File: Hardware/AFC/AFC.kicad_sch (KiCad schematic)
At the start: 102 parts, among them J1 Barrel_Jack_Switch, J2 Conn_Coaxial, J3 Conn_Coaxial, J4 Conn_Coaxial, J5 Conn_Coaxial, J7 Conn_Coaxial, J8 Conn_Coaxial, U1 AD633JRZ, U10 MC79M12_TO252, U11 LF120_TO252, U12 AD8429, U2 AD633JRZ, U3 AD630ARZ, U4 AD8429, U5 AD8429, U6 LM358, U7 LM358, U8 LM358, U9 LMV358

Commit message: Updates to schematic
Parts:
- removed J5: Conn_Coaxial, symbol Connector:Conn_Coaxial
- added C41: 100nF, symbol Device:C_Small
- R34, R5, R6: value 10k -> 100k
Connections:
- net Conventional: now also C41.1; no longer R34.2, U12.4 (+)
- net at R31.1, RV1.2, U8.6 (-): no longer RV1.1
- new net: C41.2, R34.2, U12.4 (+)
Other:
- note added: "Low Pass Filter and Output"
- note added: "Op Amp Power Supplies"
- note added: "Power Input and Regulation"
- company: (none) -> openEPR
- title: (none) -> AFC
- moved on the sheet: C23, C24, J7, J8, R12, R13, R14, R15, R16, R17, R18, R19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

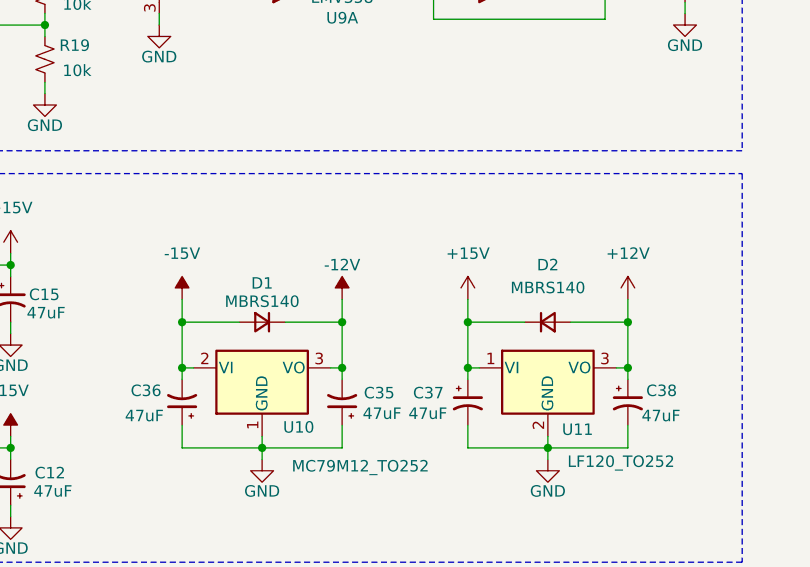
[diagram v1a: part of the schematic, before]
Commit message: Adding VCO schematic
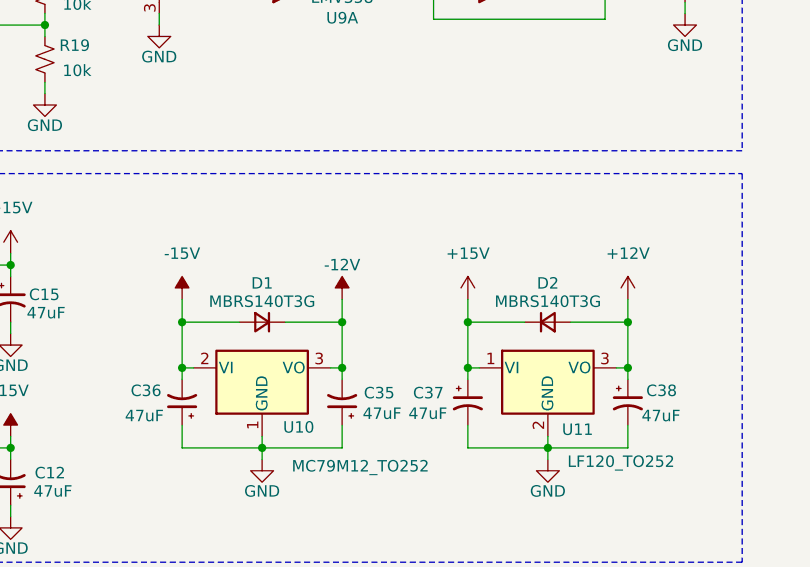
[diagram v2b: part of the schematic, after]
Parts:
- D1, D2: value MBRS140 -> MBRS140T3G
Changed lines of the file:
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@@
 			)
 		)
-		(property "Value" "MBRS140"
+		(property "Value" "MBRS140T3G"
 			(at 121.92 167.894 0)
 			(effects
@@
 		(on_board yes)
 		(dnp no)
-		(fields_autoplaced yes)
 		(property "Reference" "D2"
-			(at 153.67 163.83 0)
-			(effects
-				(font
-					(size 1.27 1.27)
-				)
-			)
-		)
-		(property "Value" "MBRS140"
-			(at 153.67 166.37 0)
-			(effects
-				(font
+			(at 153.67 165.862 0)
+			(effects
+				(font
+					(size 1.27 1.27)
+				)
+			)
+		)
+		(property "Value" "MBRS140T3G"
+			(at 153.67 167.894 0)
+			(effects
+				(font

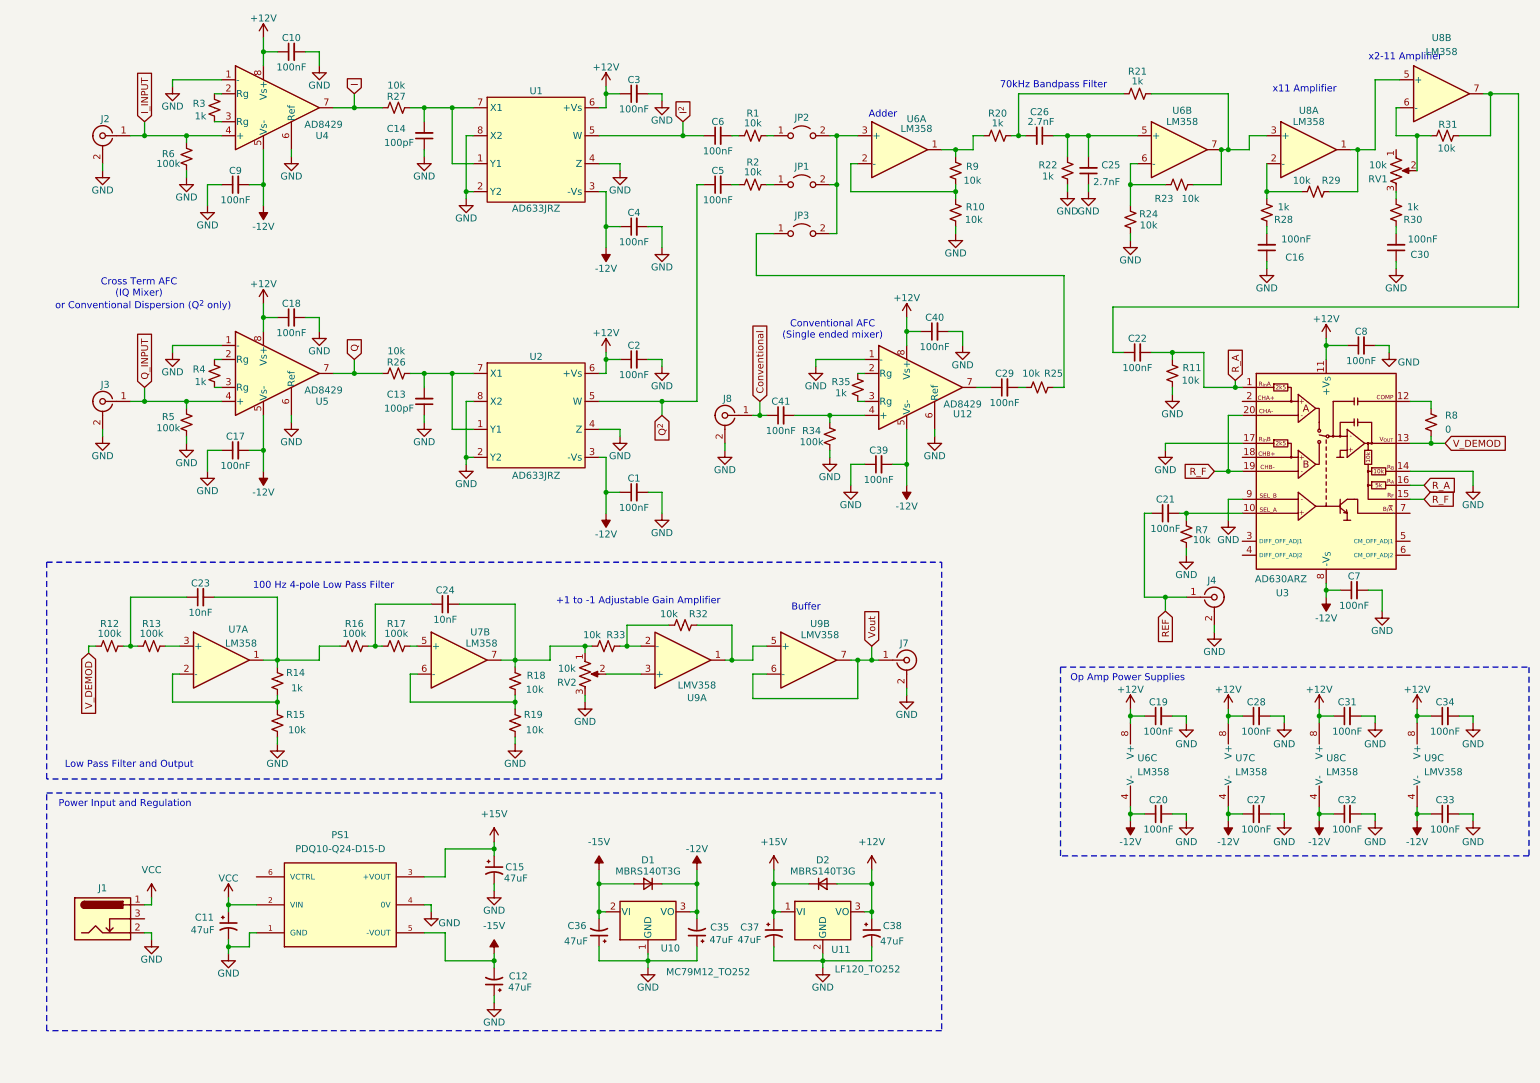
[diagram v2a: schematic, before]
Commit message: Changing to low noise op amp
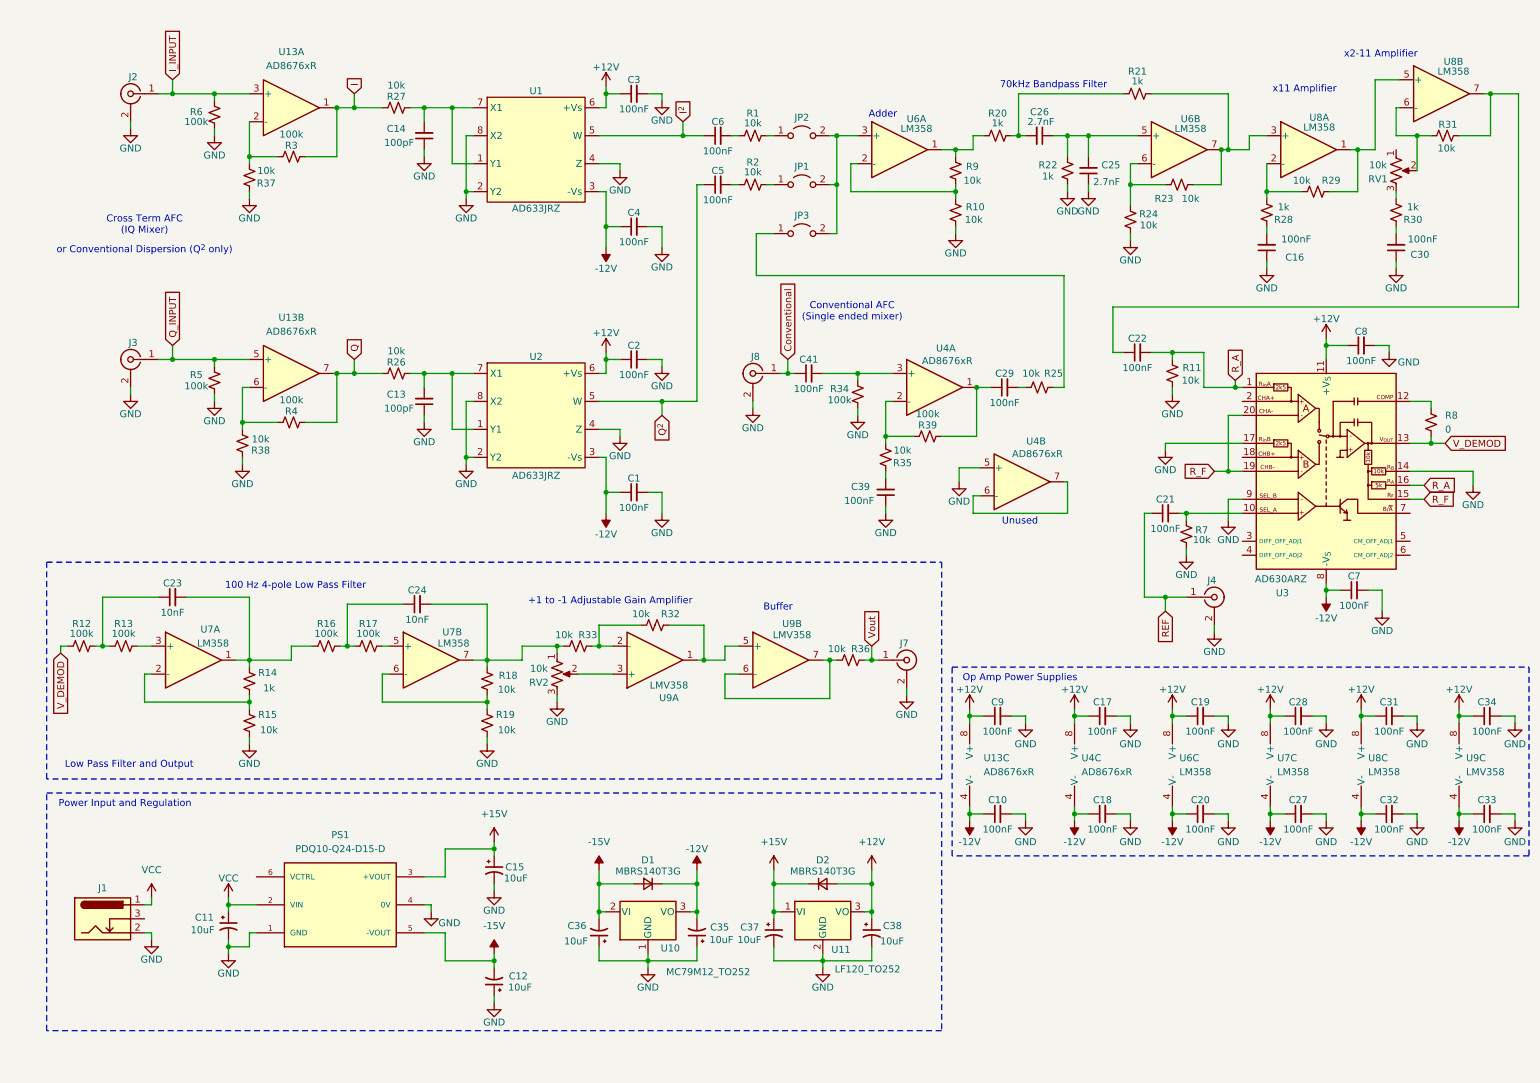
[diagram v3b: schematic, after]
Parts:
- removed C40: 100nF, symbol Device:C_Small
- removed U12, U4, U5: AD8429, symbol Amplifier_Instrumentation:AD8429
- added R36, R37, R38: 10k, symbol Device:R_Small_US
- added R39: 100k, symbol Device:R_Small_US
- added U13, U4: AD8676xR, Package_SO:SOIC-8_3.9x4.9mm_P1.27mm, symbol Amplifier_Operational:AD8676xR
- C11, C12, C15, C35, C36, C37, C38: value 47uF -> 10uF
- R3, R4: value 1k -> 100k
- R35: value 1k -> 10k
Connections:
- net +12V: now also C17.1, C9.1, U13.8 (V+), U4.8 (V+); no longer C10.1, C18.1
- net -12V: now also C10.1, C18.1, U13.4 (V-), U4.4 (V-); no longer C17.2, C39.2, C9.2
- net GND: now also C17.2, C9.2, R37.2, R38.2, U4.5 (+); no longer C17.1, C9.1
- net I: now also R3.1, U13.1
- net I_INPUT: now also U13.3 (+)
- net Q: now also R4.1, U13.7
- net Q_INPUT: now also U13.5 (+)
- net Vout: now also R36.2; no longer U9.6 (-), U9.7
- net at R35.1: now also R39.2, U4.2 (-)
- net at R35.2: now also C39.2
- net at C29.1: now also R39.1, U4.1
- net at R4.2: now also R38.1, U13.6 (-)
- net at C41.2, R34.2: now also U4.3 (+)
- net at R3.2: now also R37.1, U13.2 (-)
- new net: R36.1, U9.6 (-), U9.7
- new net: U4.6 (-), U4.7
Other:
- note added: "Unused"
- moved on the sheet: C19, C20, C23, C24, C27, C28, C31, C32, C33, C34, C41, J2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

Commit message: Adding sheets to schematic and starting PID controller
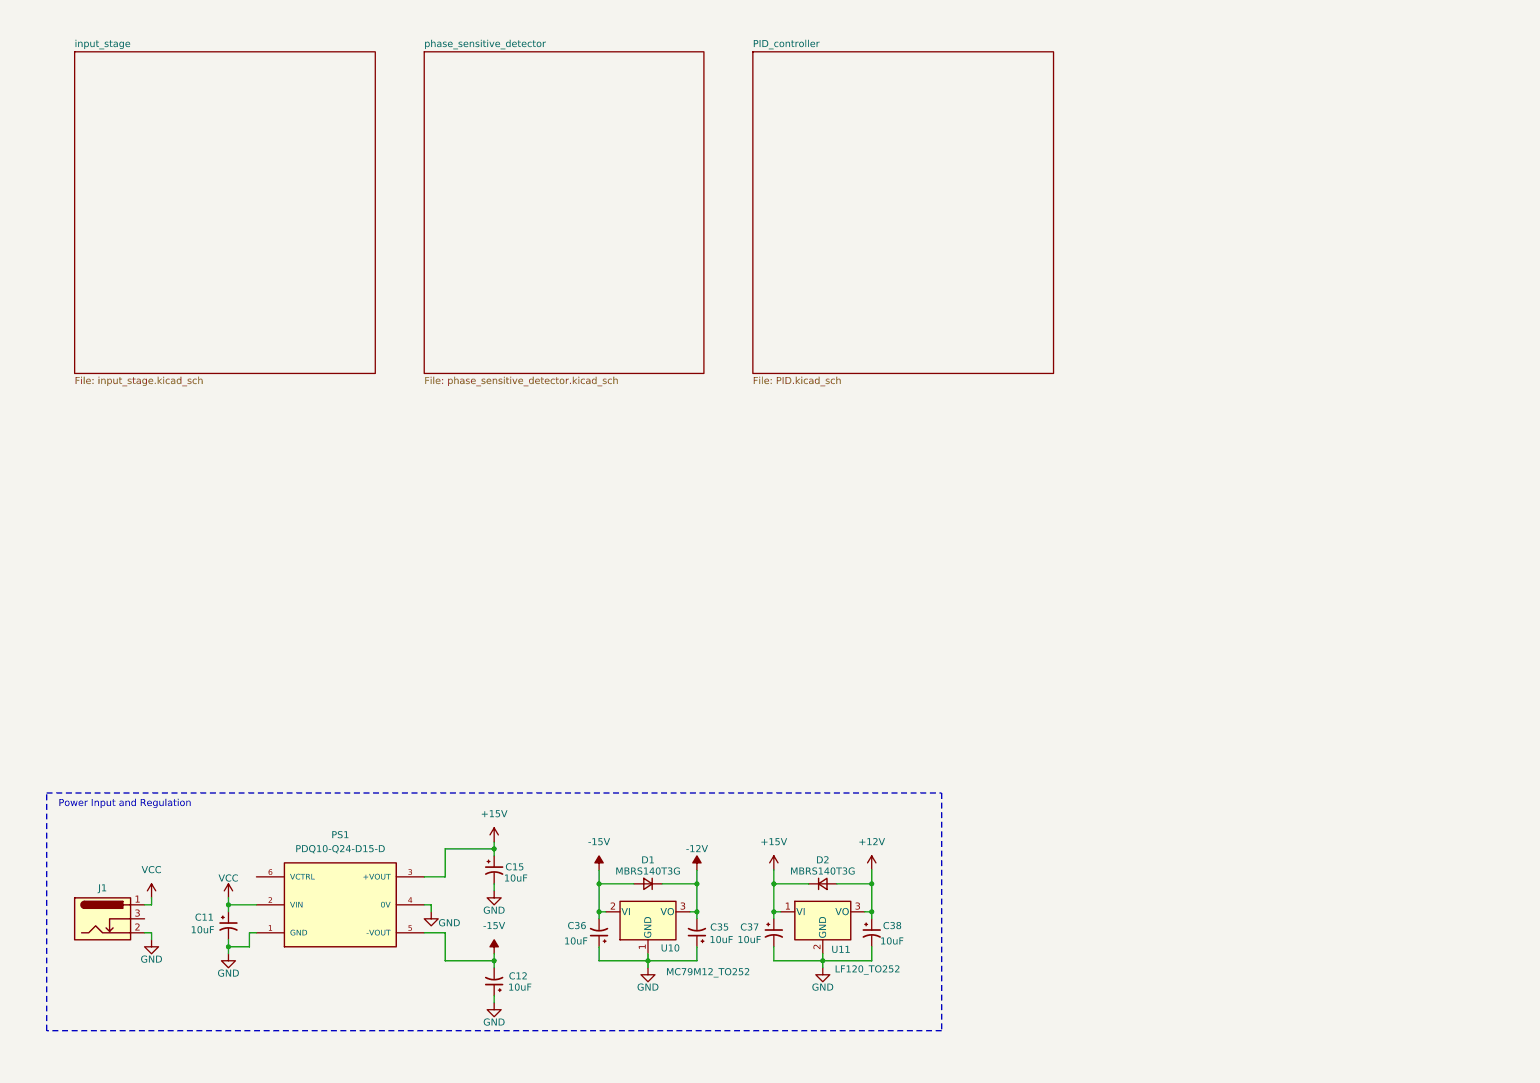
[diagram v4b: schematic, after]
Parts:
- removed C1, C10, C16, C17, C18, C19, C2, C20, C21, C22, C27, C28, C29, C3, C30, C31, C32, C33, C34, C39, C4, C41, C5, C6, C7, C8, C9: 100nF, symbol Device:C_Small
- removed C13, C14: 100pF, symbol Device:C_Small
- removed C23, C24: 10nF, symbol Device:C_Small
- removed C25, C26: 2.7nF, symbol Device:C_Small
- removed J2, J3, J4, J7, J8: Conn_Coaxial, symbol Connector:Conn_Coaxial
- removed JP1, JP2, JP3: Jumper_2_Open, symbol Jumper:Jumper_2_Open
- removed R1, R10, R11, R15, R18, R19, R2, R23, R24, R25, R26, R27, R29, R31, R32, R33, R35, R36, R37, R38, R7, R9: 10k, symbol Device:R_Small_US
- removed R12, R13, R16, R17, R3, R34, R39, R4, R5, R6: 100k, symbol Device:R_Small_US
- removed R14, R20, R21, R22, R28, R30: 1k, symbol Device:R_Small_US
- removed R8: 0, symbol Device:R_Small_US
- removed RV1, RV2: 10k, symbol Device:R_Potentiometer_US
- removed U1, U2: AD633JRZ, Package_SO:SOIC-8_3.9x4.9mm_P1.27mm, symbol _tim-RF:AD633JRZ
- removed U13, U4: AD8676xR, Package_SO:SOIC-8_3.9x4.9mm_P1.27mm, symbol Amplifier_Operational:AD8676xR
- removed U3: AD630ARZ, Package_SO:SOIC-20W_7.5x12.8mm_P1.27mm, symbol Analog:AD630ARZ
- removed U6, U7, U8: LM358, Package_SO:SOIC-8_3.9x4.9mm_P1.27mm, symbol Amplifier_Operational:LM358
- removed U9: LMV358, symbol Amplifier_Operational:LMV358
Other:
- added sheet PID_controller (PID.kicad_sch)
- added sheet input_stage (input_stage.kicad_sch)
- added sheet phase_sensitive_detector (phase_sensitive_detector.kicad_sch)
- note removed: "+1 to -1 Adjustable Gain Amplifier"
- note removed: "100 Hz 4-pole Low Pass Filter"
- note removed: "70kHz Bandpass Filter"
- note removed: "Adder"
- note removed: "Buffer"
- note removed: "Conventional AFC (Single ended mixer)"
- note removed: "Cross Term AFC (IQ Mixer)"
- note removed: "Low Pass Filter and Output"
- note removed: "Op Amp Power Supplies"
- note removed: "Unused"
- note removed: "or Conventional Dispersion (Q^{2} only)"
- note removed: "x11 Amplifier"
- note removed: "x2-11 Amplifier"
